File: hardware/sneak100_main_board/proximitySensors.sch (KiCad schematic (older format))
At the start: 23 parts, among them Q3 SFH-313FA, Q4 SFH-313FA, Q5 SFH-313FA, Q6 SFH-313FA, U6 CD4051B, U7 CD4051B

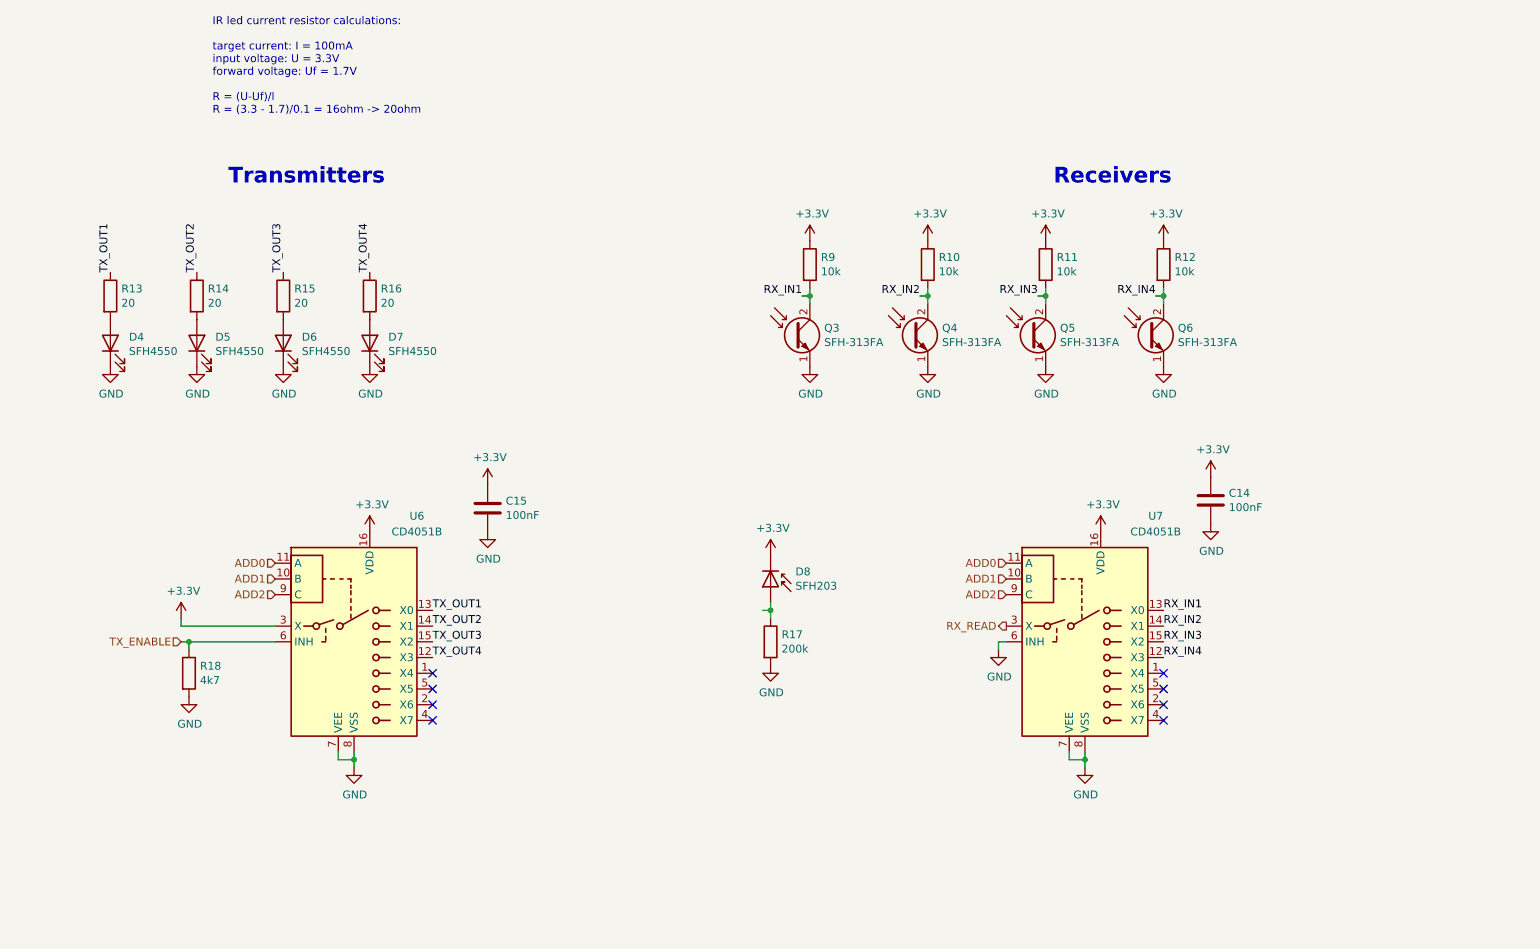
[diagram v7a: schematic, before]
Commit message: Board interface layout
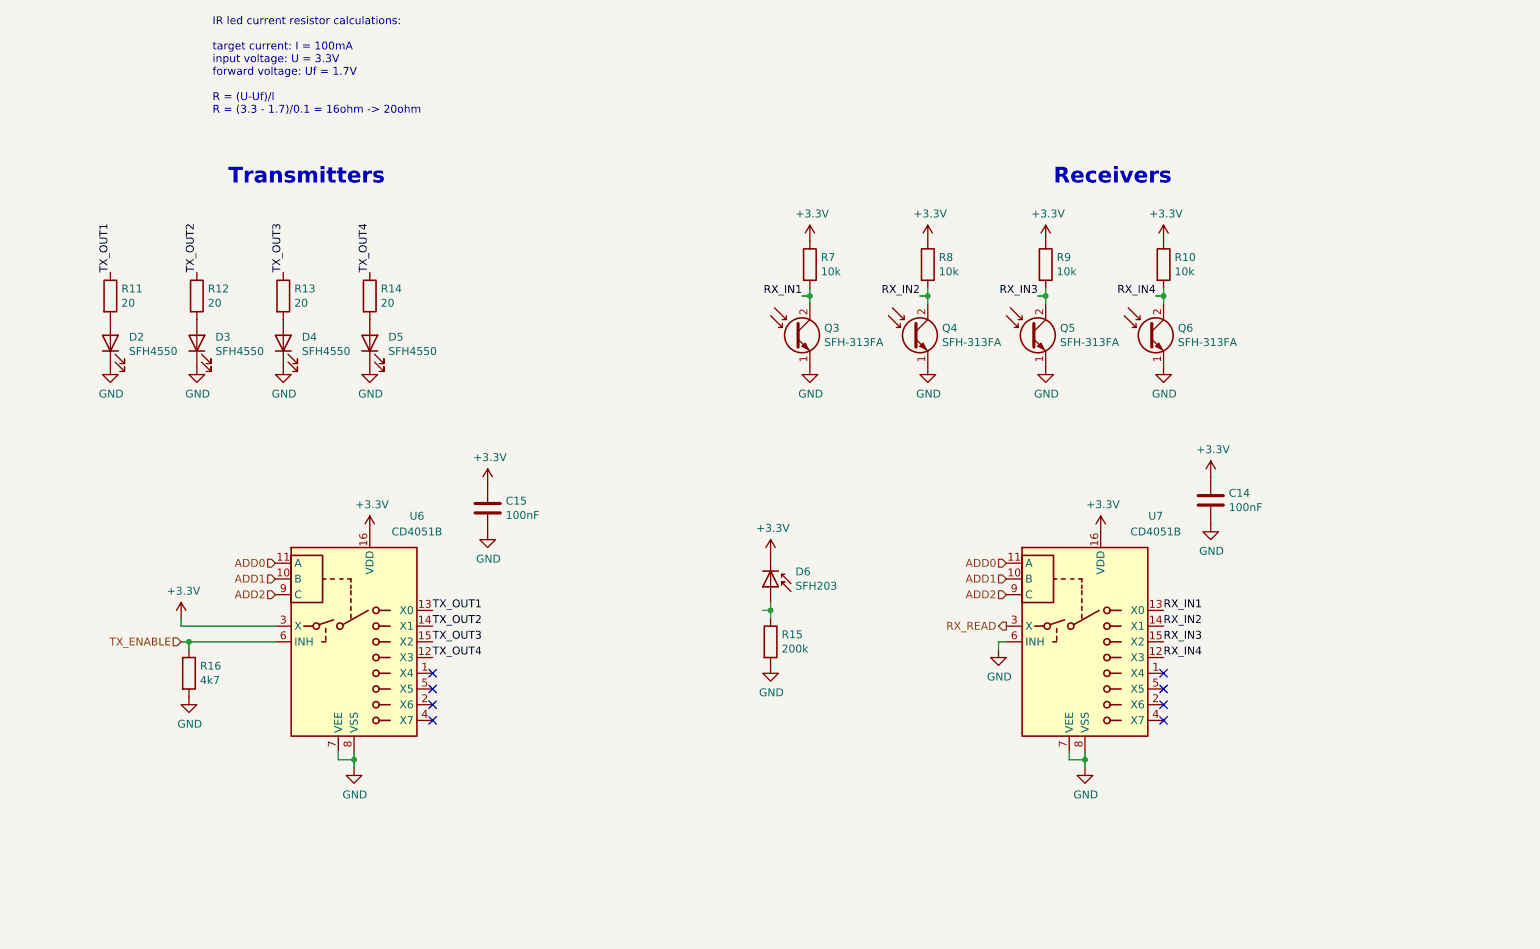
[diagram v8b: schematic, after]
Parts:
- renumbered D4 to D2, D5 to D3, D6 to D4, D7 to D5, D8 to D6, R12 to R10, R13 to R11, R14 to R12, R15 to R13, R16 to R14, R17 to R15, R18 to R16, R9 to R7, R10 to R8, R11 to R9
